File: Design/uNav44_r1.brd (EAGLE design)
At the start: 39.9 x 39.9 mm, 73 parts, among them IC1 DSPIC33FJ128MC, IC2 24LC024, IC3 AP3417CK-3.3TRG1, IC4 AP6503SP-13, U1 MCP6G01T-E/OT, U2 MCP6G01T-E/OT, U3 MCP6G01T-E/OT, U4 MCP6G01T-E/OT

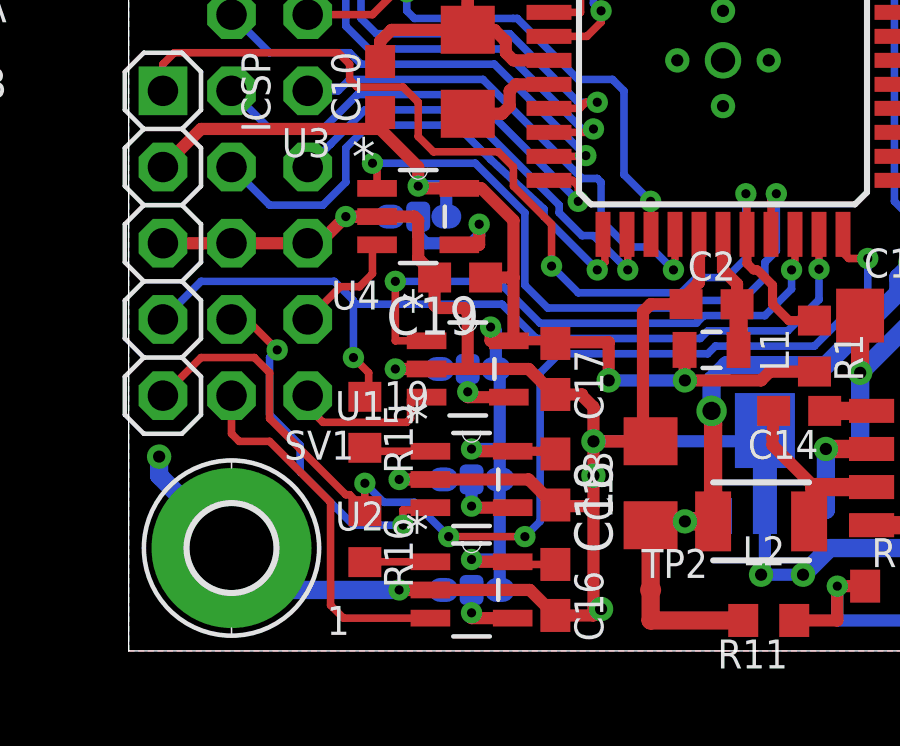
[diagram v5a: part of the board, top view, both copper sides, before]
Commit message: With a new 4-via Jumper now OA gain can be controlled by MCU
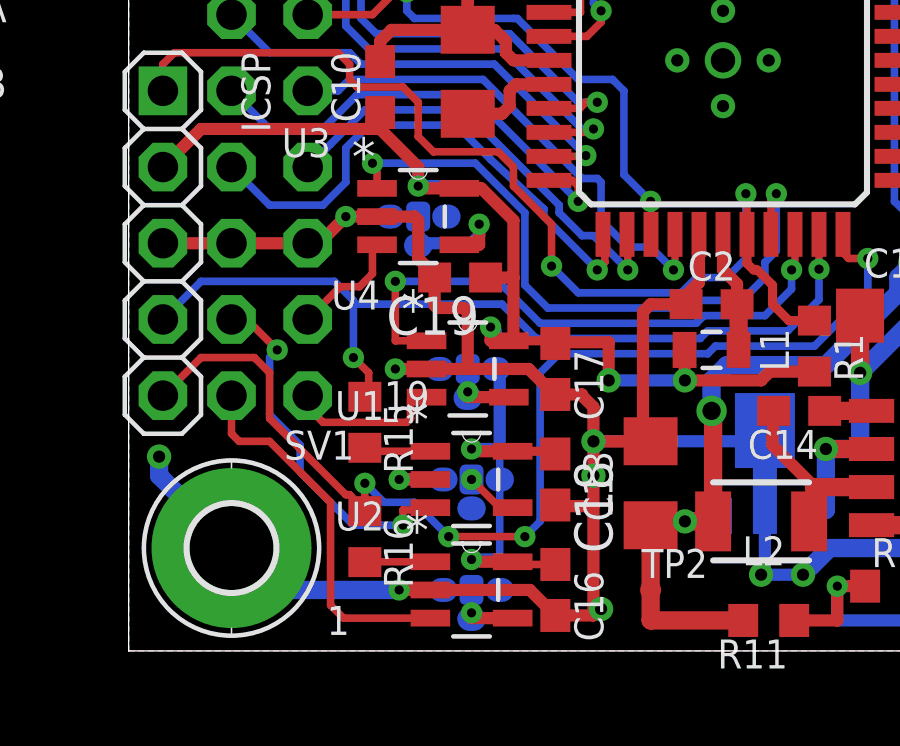
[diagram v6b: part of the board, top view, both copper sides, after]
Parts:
- removed JMP1, JMP2, JMP3, JMP4: 0R-JUMPC, jump-0r-smd:C0R-JMP
- added JP2, JP3, JP4, JP5: (no value), OfficineRobotiche:C0R-JUMP-4
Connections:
- removed net N$11: JMP1.2, U1.4
- removed net N$18: JMP2.2, U2.4
- removed net N$19: JMP3.2, U3.4
- removed net N$20: JMP4.2, U4.4
- new net GAIN_A1: JP4.2, U3.4
- new net GAIN_ANA2: JP2.2, U1.4
- new net GAIN_ANB2: JP3.2, U2.4
- new net GAIN_B1: JP5.2, U4.4
- net +3V3: now also JP2.1, JP3.1, JP4.1, JP5.1; no longer JMP1.1, JMP2.1, JMP3.1, JMP4.1
- net GND: now also JP2.3, JP3.3, JP4.3, JP5.3; no longer JMP1.3, JMP2.3, JMP3.3, JMP4.3
- net IO3: now also JP4.4
- net IO4: now also JP5.4
- net IO5: now also JP3.4
- net IO6: now also JP2.4
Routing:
- net GND: track 281.5 -> 272.6 mm
- net N$19: track 4.60 -> 0.00 mm, vias 1 -> 0
- net GAIN_A1: track 0.00 -> 4.60 mm, vias 0 -> 1
- net +3V3: track 151.4 -> 148.9 mm
- net N$18: track 2.31 -> 0.00 mm, vias 1 -> 0
- net N$11: track 2.31 -> 0.00 mm, vias 1 -> 0
- net GAIN_ANB2: track 0.00 -> 2.31 mm, vias 0 -> 1
- net N$20: track 2.31 -> 0.00 mm, vias 1 -> 0
- net GAIN_B1: track 0.00 -> 2.31 mm, vias 0 -> 1
- net GAIN_ANA2: track 0.00 -> 1.76 mm, vias 0 -> 1

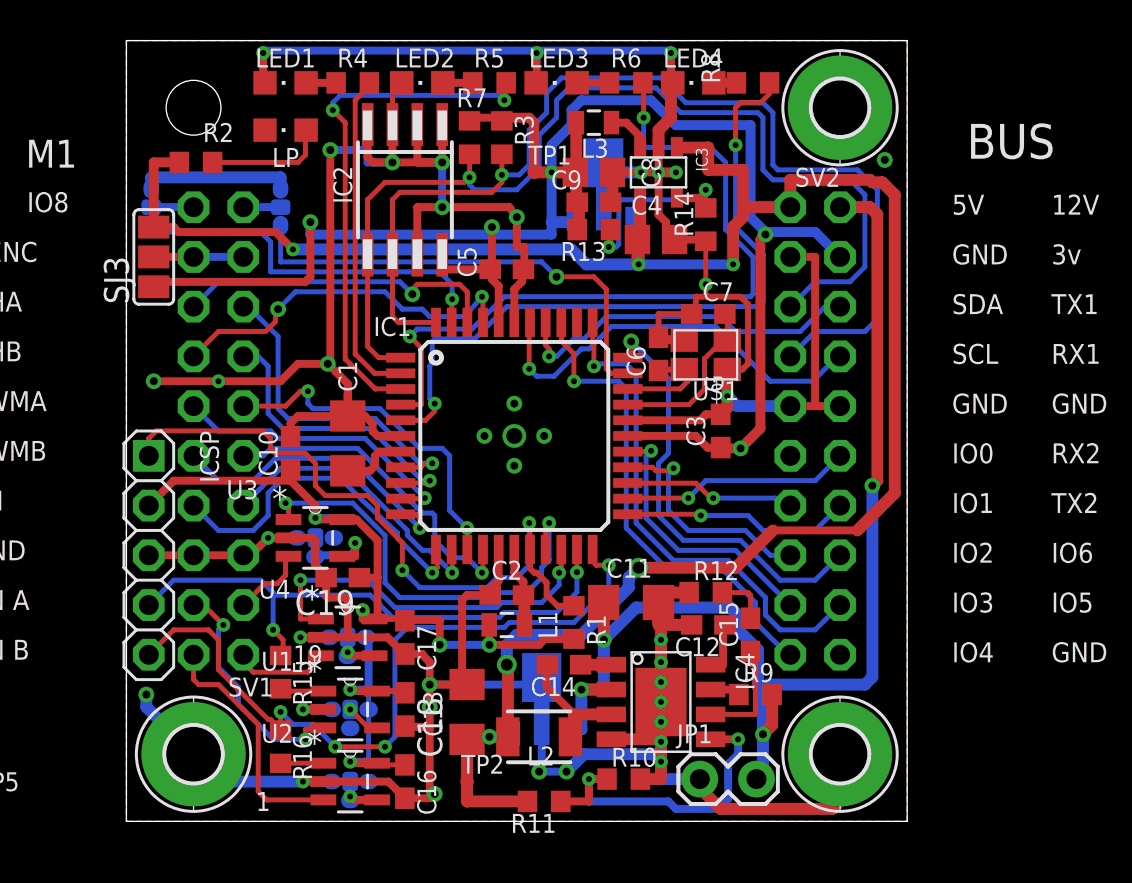
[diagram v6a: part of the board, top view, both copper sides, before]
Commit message: First release with 100% routing complete... and some error :)
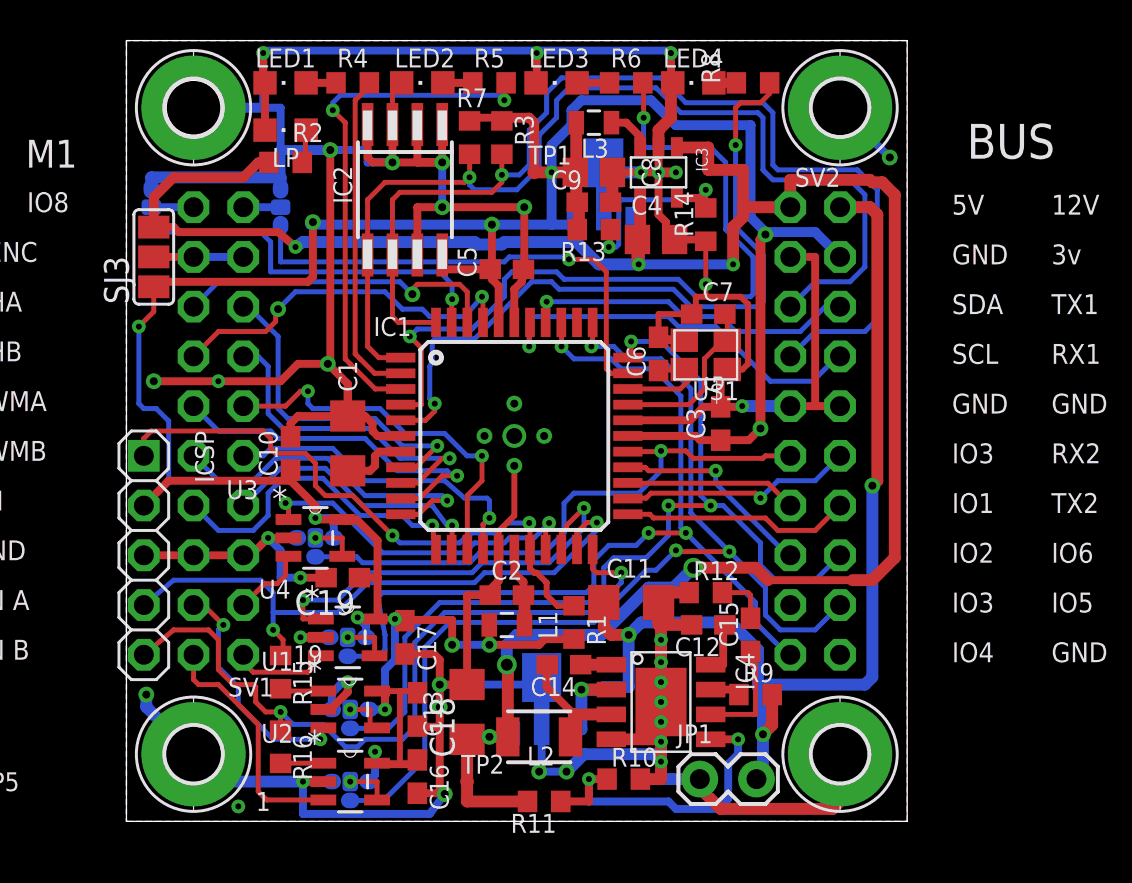
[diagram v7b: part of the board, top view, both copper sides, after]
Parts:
- added H4: MOUNT-PAD-ROUND2.8, holes:2,8-PAD
- moved R2 4.57 mm to (4.70, 30.2)
- moved C16 0.68 mm to (11.4, -1.14)
- moved C18 0.63 mm to (11.4, 2.29)
- moved C3 0.38 mm to (26.9, 16.9)
- moved ICSP 0.25 mm to (-2.54, 10.2)
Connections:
- removed net IO0: SV2.12
- net GND: now also H4.B2,8
- net IO3: now also SV2.12; no longer SV2.18
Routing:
- net GND: track 272.6 -> 302.3 mm, vias 39 -> 41
- net IO5: track 26.0 -> 53.0 mm, vias 1 -> 3
- net IO6: track 22.4 -> 48.6 mm, vias 1 -> 3
- net IO4: track 25.0 -> 46.7 mm, vias 1 -> 3
- net IO3: track 14.0 -> 30.2 mm
- net +3V3: track 148.9 -> 164.5 mm, vias 11 -> 13
- net +5V: track 116.3 -> 122.2 mm
- net ANA1: track 22.2 -> 17.5 mm
- net N$5: track 6.18 -> 2.04 mm
- net MCLR: track 34.3 -> 30.2 mm
- net PWMA2: track 15.0 -> 18.3 mm
- net GAIN_A1: track 4.60 -> 2.31 mm
- net ANA2/PGD: track 29.5 -> 31.7 mm
- net ANB1: track 19.2 -> 21.4 mm
- net CHB1: track 15.1 -> 17.1 mm
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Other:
- board text removed: "IO0"

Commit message: Update of some file
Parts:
- SV1, SV2: device con-lstb:MA10-2 -> OfficineRobotiche:MA10-2
- moved R8 0.89 mm to (28.6, 33.4), turned to 90 degrees
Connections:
- net IO3: now also SV2.18; no longer SV2.12
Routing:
- net IO3: track 30.2 -> 36.2 mm, vias 1 -> 2
- net LD4: track 37.5 -> 35.5 mm
- net IO2: track 10.5 -> 11.4 mm
- net VENC2-LD4: track 1.50 -> 2.39 mm
- net ANA1: track 17.5 -> 18.3 mm
- net ANB1: track 21.4 -> 22.1 mm
- net PWMB1: track 16.4 -> 15.7 mm
- net ANA2/PGD: track 31.7 -> 32.3 mm
- net LD3: track 40.0 -> 39.5 mm
- net PWMB2: track 17.7 -> 17.1 mm
- net PWMA2: track 18.3 -> 18.8 mm
- net CHB1: track 17.1 -> 17.6 mm
- net GND: vias 41 -> 61
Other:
- board text added: "+"
- board text added: "-"
- board text added: "1 2 3"
- board text added: "3"
- board text added: "4"
- board text added: "5"
- board text added: "CH_A"
- board text added: "CH_B"
- board text added: "GAIN CONFIG OPEN : 1 2-1 : 50 2-3 : 10 2-4 : I/O"
- board text added: "MOT1"
- board text added: "MOT2"
- board text added: "OFFICINEROBOTICHE.IT"
- board text added: "VBAT"
- board text added: "uNav44 Rel1.0"
- board text removed: "+12"
- board text removed: "+3"
- board text removed: "+5"
- board text removed: "+5V"
- board text removed: "3V"
- board text removed: "CA"
- board text removed: "CB"
- board text removed: "CZ"
- board text removed: "PA"
- board text removed: "PB"
- board text removed: "PGD"
- board text removed: "uNav44 Rel1"
- board text removed: "www.officinerobotiche.it"
